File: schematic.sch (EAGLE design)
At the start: 87 parts, among them J1 MEGAFIT-4SKT-RA, J10 JST-PA-SMT-RA-4, J11 JST-PA-SMT-RA-2, J12 JST-PA-SMT-RA-2, J14 JST-PA-SMT-RA-2, J15 JST-PA-SMT-RA-2, J17 JST-PA-SMT-RA-3, J18 JST-PA-SMT-RA-3, J19 JST-PA-SMT-RA-4, J20 JST-PA-SMT-RA-4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

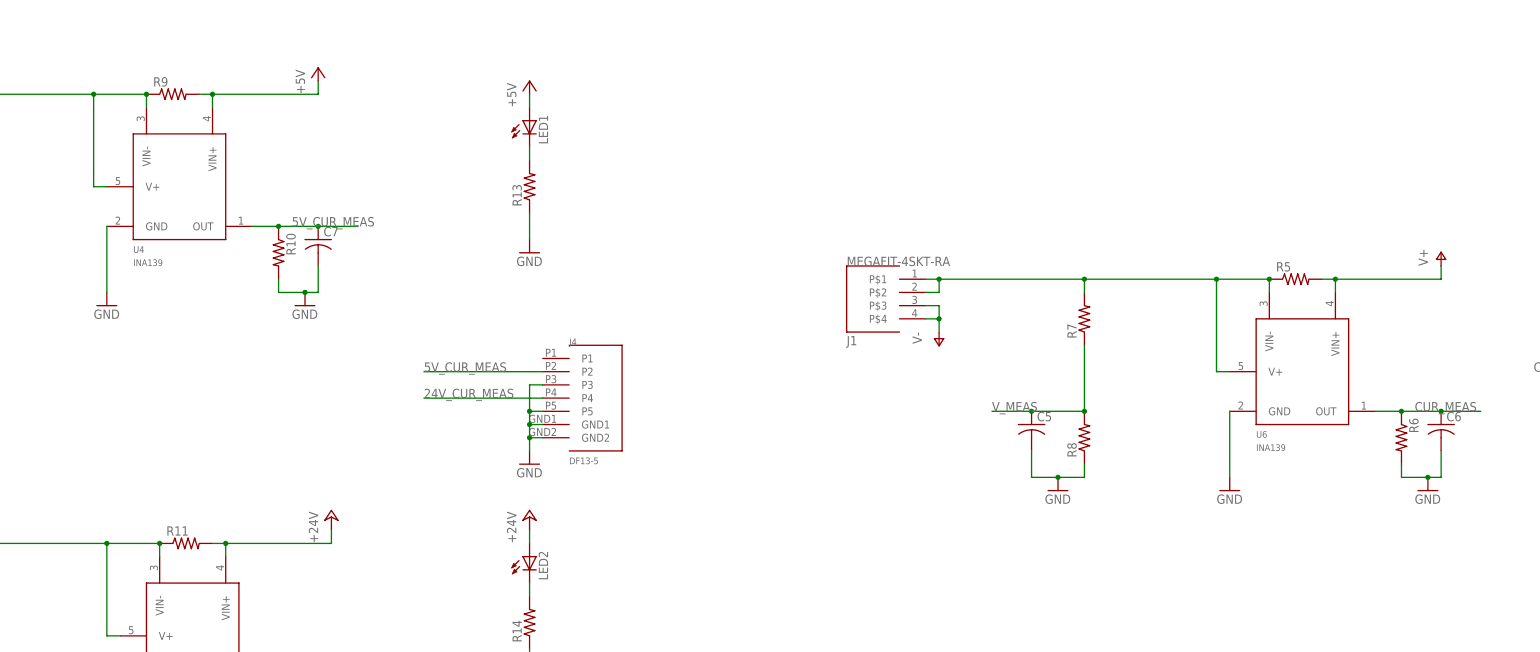
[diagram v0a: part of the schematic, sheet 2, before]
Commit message: Power traces run, remainder are low current and can be autorouted.
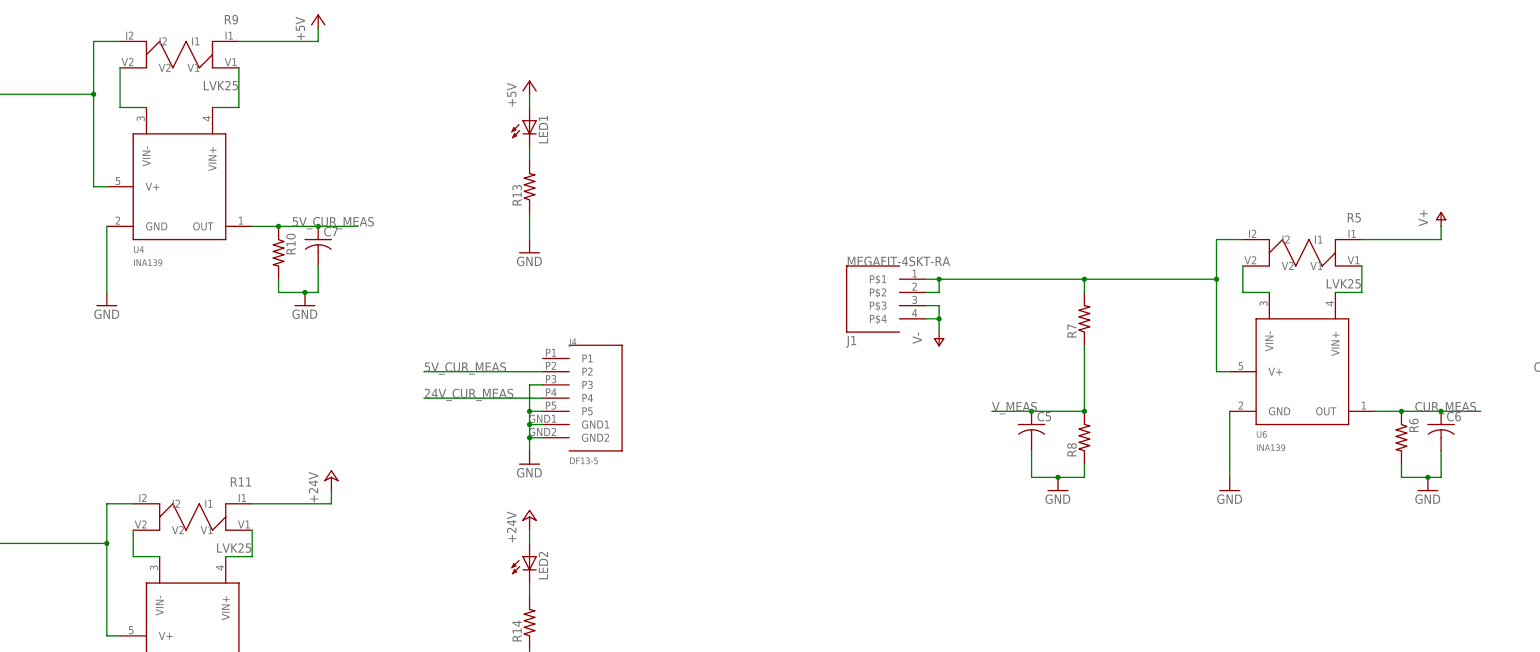
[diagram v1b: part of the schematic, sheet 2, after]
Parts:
- R11, R5, R9: value (none) -> LVK25; device rcl:R-US_M0805 -> lvk_resistor:LVK25
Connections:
- new net N$21: R1.1, R11.I2, U2.SENSE+, U2.VOUT+, U5.V+
- new net N$22: R11.V1, U5.VIN+
- new net N$23: R3.1, R9.I2, U1.SENSE+, U1.VOUT+, U4.V+
- new net N$24: R5.V2, U6.VIN-
- new net N$25: J1.P$1, J1.P$2, R5.I2, R7.2, U6.V+
- new net N$36: R5.V1, U6.VIN+
- net +24V: now also R11.I1; no longer R11.2, U5.VIN+
- net +5V: now also R9.I1; no longer R9.2, U4.VIN+
- net N$12: now also R9.V2, U4.VIN-; no longer J1.P$1, J1.P$2, R5.1, R7.2, U6.V+, U6.VIN-
- net N$13: now also R9.V1, U4.VIN+; no longer R3.1, R9.1, U1.SENSE+, U1.VOUT+, U4.V+, U4.VIN-
- net N$17: now also R11.V2; no longer R1.1, R11.1, U2.SENSE+, U2.VOUT+, U5.V+
- net V+: now also R5.I1; no longer R5.2, U6.VIN+

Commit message: Silkscreen adjustments, cleanup prior to autoroute.
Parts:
- added H1: MOUNT-PAD-ROUND3.2, holes:MOUNT-PAD-ROUND3.2
- added R16, R17, R18: (no value), rcl:R-US_M0805
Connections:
- new net N$37: H1.MOUNT, R18.2
- new net N$38: R17.2, SW2.GND1, SW2.GND2, SW2.GND3, SW2.GND4
- new net N$39: R16.2, SW1.GND1, SW1.GND2, SW1.GND3, SW1.GND4
- net GND: now also R16.1, R17.1, R18.1; no longer SW1.GND1, SW1.GND2, SW1.GND3, SW1.GND4, SW2.GND1, SW2.GND2, SW2.GND3, SW2.GND4
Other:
- note added: "Chassis Ground Pad"
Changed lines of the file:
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@@
 <part name="R9" library="lvk_resistor" deviceset="LVK25" device=""/>
 <part name="R5" library="lvk_resistor" deviceset="LVK25" device=""/>
+<part name="R16" library="rcl" deviceset="R-US_" device="M0805"/>
+<part name="R17" library="rcl" deviceset="R-US_" device="M0805"/>
+<part name="R18" library="rcl" deviceset="R-US_" device="M0805"/>
+<part name="H1" library="holes" deviceset="MOUNT-PAD-ROUND" device="3.2"/>
+<part name="GND8" library="supply1" deviceset="GND" device=""/>
 </parts>
 <sheets>
@@
 <sheet>
 <plain>
+<text x="147.32" y="35.56" size="1.778" layer="97">Chassis Ground Pad</text>
 </plain>
 <instances>
@@
 <instance part="GND26" gate="1" x="-111.76" y="93.98"/>
 <instance part="P+3" gate="1" x="-81.28" y="119.38"/>
-<instance part="GND27" gate="1" x="-129.54" y="81.28"/>
-<instance part="GND28" gate="1" x="-127" y="2.54"/>
+<instance part="GND27" gate="1" x="-129.54" y="68.58"/>
+<instance part="GND28" gate="1" x="-127" y="-10.16"/>
 <instance part="U2" gate="G$1" x="-43.18" y="20.32"/>
 <instance part="J1" gate="G$1" x="175.26" y="78.74"/>
@@
 <instance part="R9" gate="G$1" x="35.56" y="127" rot="R180"/>
 <instance part="R5" gate="G$1" x="251.46" y="88.9" rot="R180"/>
+<instance part="R16" gate="G$1" x="-129.54" y="78.74" rot="R90"/>
+<instance part="R17" gate="G$1" x="-127" y="0" rot="R90"/>
+<instance part="R18" gate="G$1" x="147.32" y="20.32" rot="R90"/>
+<instance part="H1" gate="G$1" x="149.86" y="30.48"/>
+<instance part="GND8" gate="1" x="147.32" y="10.16"/>
 </instances>
 <busses>
@@
 </segment>
 <segment>
-<pinref part="SW1" gate="G$1" pin="GND1"/>
-<pinref part="GND27" gate="1" pin="GND"/>
-<wire x1="-127" y1="93.98" x2="-129.54" y2="93.98" width="0.1524" layer="91"/>
-<wire x1="-129.54" y1="93.98" x2="-129.54" y2="91.44" width="0.1524" layer="91"/>
-<pinref part="SW1" gate="G$1" pin="GND2"/>
-<wire x1="-129.54" y1="91.44" x2="-129.54" y2="88.9" width="0.1524" layer="91"/>
-<wire x1="-129.54" y1="88.9" x2="-129.54" y2="86.36" width="0.1524" layer="91"/>
-<wire x1="-129.54" y1="86.36" x2="-129.54" y2="83.82" width="0.1524" layer="91"/>
-<wire x1="-127" y1="91.44" x2="-129.54" y2="91.44" width="0.1524" layer="91"/>
-<junction x="-129.54" y="91.44"/>
-<pinref part="SW1" gate="G$1" pin="GND3"/>
-<wire x1="-127" y1="88.9" x2="-129.54" y2="88.9" width="0.1524" layer="91"/>
-<junction x="-129.54" y="88.9"/>
-<pinref part="SW1" gate="G$1" pin="GND4"/>
-<wire x1="-127" y1="86.36" x2="-129.54" y2="86.36" width="0.1524" layer="91"/>
-<junction x="-129.54" y="86.36"/>
-</segment>
-<segment>
 <pinref part="SW2" gate="G$1" pin="NO"/>
 <pinref part="GND25" gate="1" pin="GND"/>
@@
 </segment>
 <segment>
-<pinref part="SW2" gate="G$1" pin="GND4"/>
+<pinref part="GND8" gate="1" pin="GND"/>
+<pinref part="R18" gate="G$1" pin="1"/>
+<wire x1="147.32" y1="12.7" x2="147.32" y2="15.24" width="0.1524" layer="91"/>
+</segment>
+<segment>
 <pinref part="GND28" gate="1" pin="GND"/>
-<wire x1="-124.46" y1="7.62" x2="-127" y2="7.62" width="0.1524" layer="91"/>
-<wire x1="-127" y1="7.62" x2="-127" y2="5.08" width="0.1524" layer="91"/>
-<pinref part="SW2" gate="G$1" pin="GND3"/>
-<wire x1="-124.46" y1="10.16" x2="-127" y2="10.16" width="0.1524" layer="91"/>
-<wire x1="-127" y1="10.16" x2="-127" y2="7.62" width="0.1524" layer="91"/>
-<junction x="-127" y="7.62"/>
-<pinref part="SW2" gate="G$1" pin="GND2"/>
-<wire x1="-124.46" y1="12.7" x2="-127" y2="12.7" width="0.1524" layer="91"/>
-<wire x1="-127" y1="12.7" x2="-127" y2="10.16" width="0.1524" layer="91"/>
-<junction x="-127" y="10.16"/>
-<pinref part="SW2" gate="G$1" pin="GND1"/>
-<wire x1="-124.46" y1="15.24" x2="-127" y2="15.24" width="0.1524" layer="91"/>
-<wire x1="-127" y1="15.24" x2="-127" y2="12.7" width="0.1524" layer="91"/>
-<junction x="-127" y="12.7"/>
+<pinref part="R17" gate="G$1" pin="1"/>
+<wire x1="-127" y1="-7.62" x2="-127" y2="-5.08" width="0.1524" layer="91"/>
+</segment>
+<segment>
+<pinref part="R16" gate="G$1" pin="1"/>
+<pinref part="GND27" gate="1" pin="GND"/>
+<wire x1="-129.54" y1="73.66" x2="-129.54" y2="71.12" width="0.1524" layer="91"/>
 </segment>
 </net>
@@
 </segment>
 </net>
+<net name="N$37" class="0">
+<segment>
+<pinref part="H1" gate="G$1" pin="MOUNT"/>
+<pinref part="R18" gate="G$1" pin="2"/>
+<wire x1="147.32" y1="30.48" x2="147.32" y2="25.4" width="0.1524" layer="91"/>
+</segment>
+</net>
+<net name="N$38" class="0">
+<segment>
+<pinref part="SW2" gate="G$1" pin="GND4"/>
+<wire x1="-124.46" y1="7.62" x2="-127" y2="7.62" width="0.1524" layer="91"/>
+<pinref part="SW2" gate="G$1" pin="GND3"/>
+<wire x1="-124.46" y1="10.16" x2="-127" y2="10.16" width="0.1524" layer="91"/>
+<wire x1="-127" y1="10.16" x2="-127" y2="7.62" width="0.1524" layer="91"/>
+<pinref part="SW2" gate="G$1" pin="GND2"/>
+<wire x1="-124.46" y1="12.7" x2="-127" y2="12.7" width="0.1524" layer="91"/>
+<wire x1="-127" y1="12.7" x2="-127" y2="10.16" width="0.1524" layer="91"/>
+<junction x="-127" y="10.16"/>
+<pinref part="SW2" gate="G$1" pin="GND1"/>
+<wire x1="-124.46" y1="15.24" x2="-127" y2="15.24" width="0.1524" layer="91"/>
+<wire x1="-127" y1="15.24" x2="-127" y2="12.7" width="0.1524" layer="91"/>
+<junction x="-127" y="12.7"/>
+<pinref part="R17" gate="G$1" pin="2"/>
+<wire x1="-127" y1="5.08" x2="-127" y2="7.62" width="0.1524" layer="91"/>
+<junction x="-127" y="7.62"/>
+</segment>
+</net>
+<net name="N$39" class="0">
+<segment>
+<pinref part="SW1" gate="G$1" pin="GND1"/>
+<wire x1="-127" y1="93.98" x2="-129.54" y2="93.98" width="0.1524" layer="91"/>
+<wire x1="-129.54" y1="93.98" x2="-129.54" y2="91.44" width="0.1524" layer="91"/>
+<pinref part="SW1" gate="G$1" pin="GND2"/>
+<wire x1="-129.54" y1="91.44" x2="-129.54" y2="88.9" width="0.1524" layer="91"/>
+<wire x1="-129.54" y1="88.9" x2="-129.54" y2="86.36" width="0.1524" layer="91"/>
+<wire x1="-127" y1="91.44" x2="-129.54" y2="91.44" width="0.1524" layer="91"/>
+<junction x="-129.54" y="91.44"/>
+<pinref part="SW1" gate="G$1" pin="GND3"/>
+<wire x1="-127" y1="88.9" x2="-129.54" y2="88.9" width="0.1524" layer="91"/>
+<junction x="-129.54" y="88.9"/>
+<pinref part="SW1" gate="G$1" pin="GND4"/>
+<wire x1="-127" y1="86.36" x2="-129.54" y2="86.36" width="0.1524" layer="91"/>
+<pinref part="R16" gate="G$1" pin="2"/>
+<wire x1="-129.54" y1="83.82" x2="-129.54" y2="86.36" width="0.1524" layer="91"/>
+<junction x="-129.54" y="86.36"/>
+</segment>
+</net>
